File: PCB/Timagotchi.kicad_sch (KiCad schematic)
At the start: 11 parts, among them J1 Conn_01x13_Pin, J2 Conn_01x02_Pin, SW1 SW_Omron_B3FS, SW2 SW_Omron_B3FS, SW3 SW_Omron_B3FS, SW4 SW_Omron_B3FS, SW5 SW_Omron_B3FS, SW6 SW_Omron_B3FS, U1 XIAO-ESP32-S3-Plus-SMD, U2 MAX98357A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

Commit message: puhcuhbuh
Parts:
- removed J1: Conn_01x13_Pin, Connector_JST:JST_SH_SM13B-SRSS-TB_1x13-1MP_P1.00mm_Horizontal, symbol Connector:Conn_01x13_Pin
- added J3: 2005280180, CON_2005280180_MOL, symbol FFC:2005280180
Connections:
- net +3.3V: now also J3.1
- net GND: now also J3.3, J3.P1, J3.P2
- net LCD_BL: now also J3.2
- net LCD_CS: now also J3.9
- net LCD_DC: now also J3.7
- net LCD_RST: now also J3.8
- net MOSI: now also J3.5
- net SCLK: now also J3.4
- net TP_INT: now also J3.15
- net TP_SCL: now also J3.13
- net TP_SDA: now also J3.14
- net +5V: now reaches U1.14 (VBUS)
- new net MISO: J3.6
- no-connect marks 7 -> 14
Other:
- note added: "Screen FFC connector"
- note removed: "Screen Connector"

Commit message: optimizations and other stuff.
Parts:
- removed SW4, SW5, SW6: SW_Omron_B3FS, Button_Switch_SMD:SW_SPST_Omron_B3FS-100xP, symbol Switch:SW_Omron_B3FS
- J3: footprint CON_2005280180_MOL -> Connector_FFC-FPC:Molex_200528-0180_1x18-1MP_P1.00mm_Horizontal
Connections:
- net SD_CS is gone; now on net MOSI: U1.2 (GPIO2_A1_D1)
- net SW4 is gone; now on net LCD_CS: U1.18 (GPIO41_PDM_DATA_RX1)
- net SW5 is gone; now on net HPOS: U1.19 (GPIO42_PDM_CLK_TX1)
- net SW6 is gone; now on net VPOS: U1.20 (GPIO10_XMCLK_ADC_BAT)
- net TP_RST is gone; now on net I2S_SD: U1.10 (GPIO8_A9_D9_MISO)
- net HPOS: no longer U1.28 (GPIO42_MTMS_PDM_CLK_TX1)
- net I2S_SCK: now also U1.22 (GPIO12_DVP_Y7_SPI_MISO1); no longer U1.16 (GPIO39_CAM_SCL_I2S_SCK)
- net I2S_SD: no longer U1.15 (GPIO38_DVP_VSYNC_I2S_SD)
- net I2S_WS: now also U1.9 (GPIO7_A8_D8_SCK); no longer U1.17 (GPIO40_CAM_SDA_I2S_WS)
- net LCD_CS: no longer U1.8 (GPIO44_D7_RX)
- net MOSI: no longer U1.11 (GPIO9_A10_D10_MOSI)
- net SCLK: now also U1.17 (GPIO40_CAM_SDA_I2S_WS); no longer U1.9 (GPIO7_A8_D8_SCK)
- net SEL: now also U1.11 (GPIO9_A10_D10_MOSI); no longer U1.25 (GPIO40_MTDO_CAM_SDA_I2S_WS)
- net SW1: now also U1.8 (GPIO44_D7_RX); no longer U1.21 (GPIO11_DVP_Y8_SPI_MOSI1)
- net SW2: now also U1.21 (GPIO11_DVP_Y8_SPI_MOSI1); no longer U1.22 (GPIO12_DVP_Y7_SPI_MISO1)
- net VPOS: no longer U1.29 (GPIO39_MTCK_CAM_SCL_I2S_SCK)
- no-connect marks 14 -> 17

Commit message: Pcb changes, mostly files and 3d models.
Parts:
- removed U3: COM-09032, Joystick footprint:XDCR_COM-09032, symbol COM-09032:COM-09032
- added J1: Conn_01x04, Library:JOYSTICK-PSP1000, symbol Connector_Generic:Conn_01x04
- ScreenConnector: renamed from J3; footprint Connector_FFC-FPC:Molex_200528-0180_1x18-1MP_P1.00mm_Horizontal -> FFC:CON_2005280180_MOL
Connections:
- net +3.3V: now also J1.4 (Pin_4)
- net GND: now also J1.2 (Pin_2)
- net HPOS: now also U1.20 (GPIO10_XMCLK_ADC_BAT), J1.1 (Pin_1); no longer U1.19 (GPIO42_PDM_CLK_TX1)
- net VPOS: now also U1.19 (GPIO42_PDM_CLK_TX1), J1.3 (Pin_3); no longer U1.20 (GPIO10_XMCLK_ADC_BAT)
- net SEL: no longer names the net of U1.11 (GPIO9_A10_D10_MOSI)
- no-connect marks 17 -> 18

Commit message: puh cuh buh 2
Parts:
- renumbered ScreenConnector to ScreenConnector1
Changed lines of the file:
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@@
 		(dnp no)
 		(fields_autoplaced yes)
-		(property "Reference" "ScreenConnector"
+		(property "Reference" "ScreenConnector1"
 			(at 171.45 53.3399 0)
 			(show_name no)
@@
 			(project "Timagotchi"
 				(path "/fffb594e-bf77-45e9-a4da-34b8c4c79703"
-					(reference "ScreenConnector")
+					(reference "ScreenConnector1")
 					(unit 1)
 				)

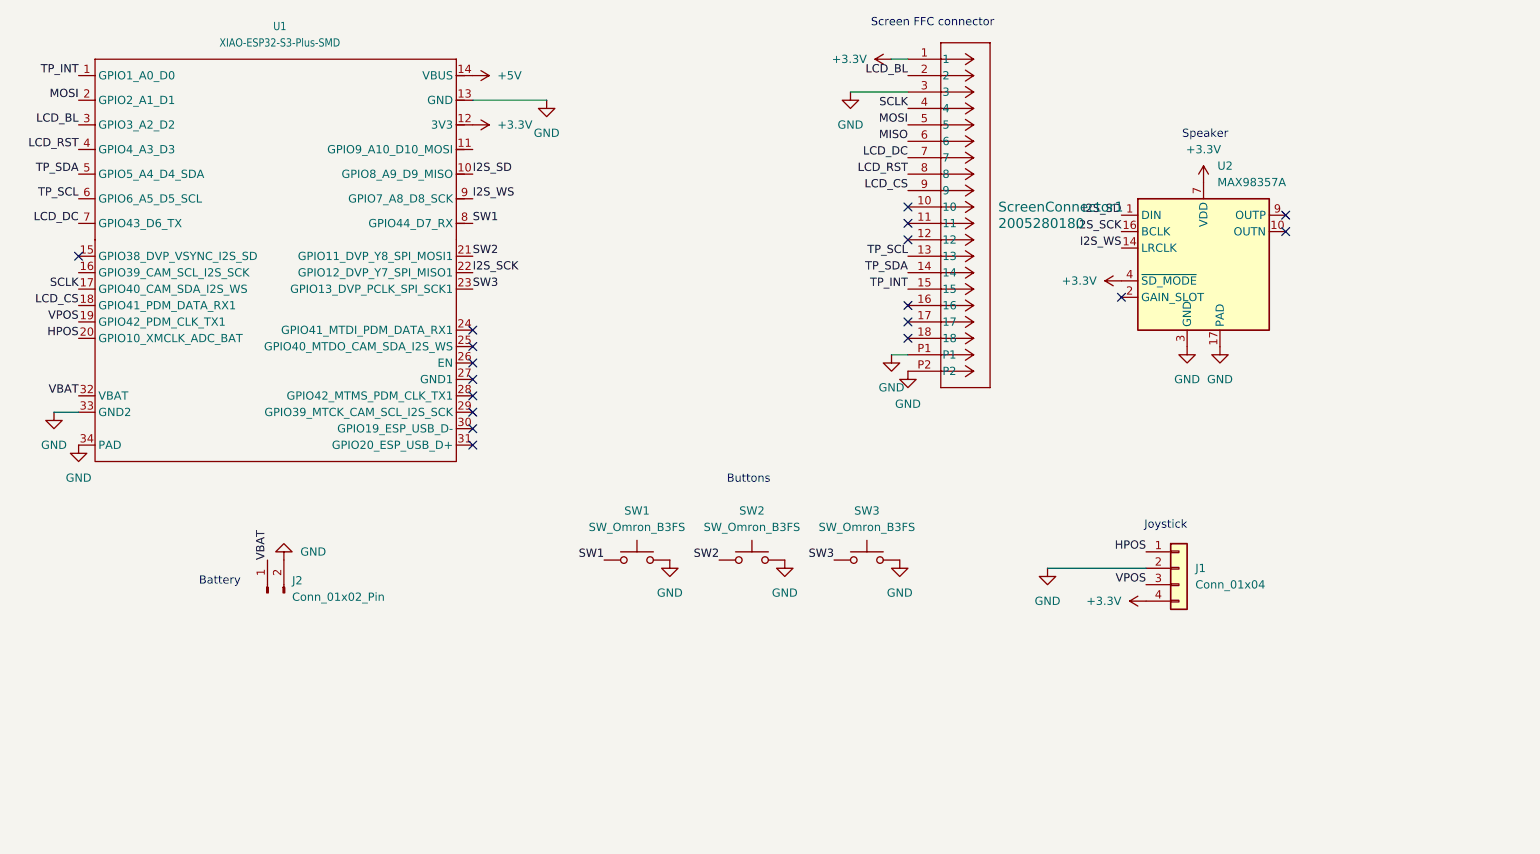
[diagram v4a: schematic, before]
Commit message: wiring and new speaker
added CMS-201438-058S
speaker and new gpio wiring
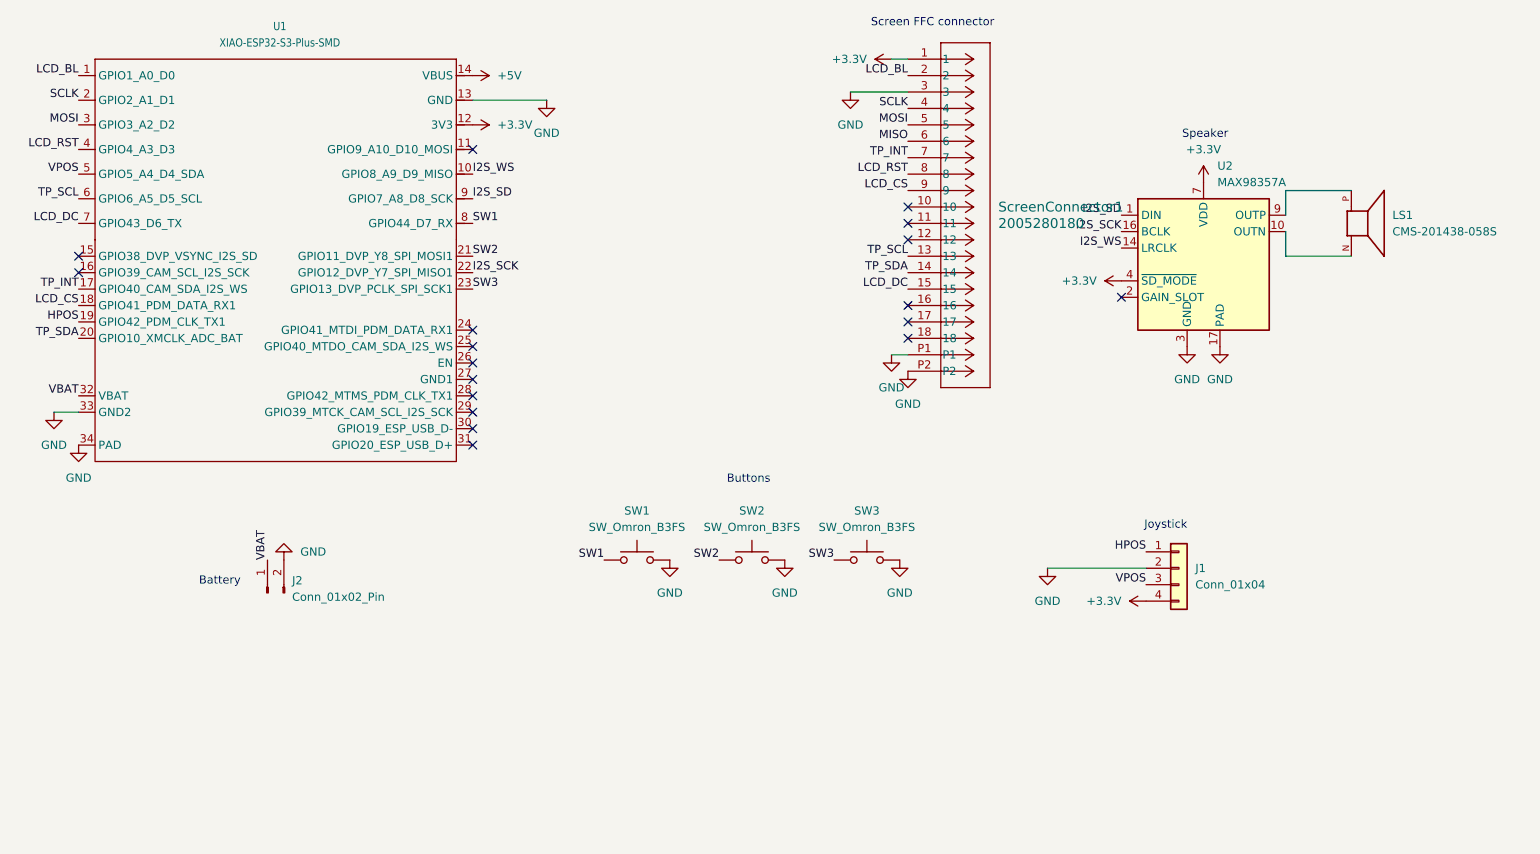
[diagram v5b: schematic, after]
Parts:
- added LS1: CMS-201438-058S, Speaker speaker:SPKR_CMS-201438-058S, symbol CMS-201438-058S:CMS-201438-058S
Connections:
- net HPOS: now also U1.19 (GPIO42_PDM_CLK_TX1); no longer U1.20 (GPIO10_XMCLK_ADC_BAT)
- net I2S_SD: now also U1.9 (GPIO7_A8_D8_SCK); no longer U1.10 (GPIO8_A9_D9_MISO)
- net I2S_WS: now also U1.10 (GPIO8_A9_D9_MISO); no longer U1.9 (GPIO7_A8_D8_SCK)
- net LCD_BL: now also U1.1 (GPIO1_A0_D0); no longer U1.3 (GPIO3_A2_D2)
- net LCD_DC: now also ScreenConnector1.15; no longer ScreenConnector1.7
- net MOSI: now also U1.3 (GPIO3_A2_D2); no longer U1.2 (GPIO2_A1_D1)
- net SCLK: now also U1.2 (GPIO2_A1_D1); no longer U1.17 (GPIO40_CAM_SDA_I2S_WS)
- net TP_INT: now also ScreenConnector1.7, U1.17 (GPIO40_CAM_SDA_I2S_WS); no longer ScreenConnector1.15, U1.1 (GPIO1_A0_D0)
- net TP_SDA: now also U1.20 (GPIO10_XMCLK_ADC_BAT); no longer U1.5 (GPIO5_A4_D4_SDA)
- net VPOS: now also U1.5 (GPIO5_A4_D4_SDA); no longer U1.19 (GPIO42_PDM_CLK_TX1)
- net at U2.10 (OUTN): now also LS1.N
- net at U2.9 (OUTP): now also LS1.P
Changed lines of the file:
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@@
-	)
-	(no_connect
-		(at 215.9 54.61)
 	)
 	(no_connect
@@
 	)
 	(no_connect
-		(at 215.9 57.15)
-	)
-	(no_connect
 		(at 157.48 53.34)
 	)
@@
 	(no_connect
 		(at 90.17 87.63)
+	)
+	(no_connect
+		(at 90.17 44.45)
+	)
+	(no_connect
+		(at 29.21 63.5)
 	)
 	(no_connect
@@
 	(wire
 		(pts
-			(xy 154.94 76.2) (xy 157.48 76.2)
+			(xy 215.9 54.61) (xy 215.9 50.8)
 		)
 		(stroke
@@
 	(wire
 		(pts
-			(xy 25.4 85.09) (xy 29.21 85.09)
+			(xy 215.9 60.96) (xy 215.9 57.15)
 		)
 		(stroke
@@
 	(wire
 		(pts
-			(xy 148.59 35.56) (xy 157.48 35.56)
+			(xy 154.94 76.2) (xy 157.48 76.2)
 		)
 		(stroke
@@
 		)
 	)
+	(wire
+		(pts
+			(xy 215.9 50.8) (xy 226.06 50.8)
+		)
+		(stroke
+			(width 0)
+			(type default)
+		)
+	)
+	(wire
+		(pts
+			(xy 25.4 85.09) (xy 29.21 85.09)
+		)
+		(stroke
+			(width 0)
+			(type default)
+		)
+	)
+	(wire
+		(pts
+			(xy 148.59 35.56) (xy 157.48 35.56)
+		)
+		(stroke
+			(width 0)
+			(type default)
+		)
+	)
+	(wire
+		(pts
+			(xy 226.06 60.96) (xy 215.9 60.96)
+		)
+		(stroke
+			(width 0)
+			(type default)
+		)
+	)
 	(label "VBAT"
 		(at 29.21 82.55 180)
@@
 		)
 	)
-	(label "SCLK"
+	(label "TP_INT"
 		(at 29.21 66.04 180)
 		(effects
@@
 		)
 	)
-	(label "HPOS"
+	(label "TP_SDA"
 		(at 29.21 73.66 180)
 		(effects
@@
 		)
 	)
+	(label "MOSI"
+		(at 29.21 40.64 180)
+		(effects
+			(font
+				(size 1.27 1.27)
+			)
+			(justify right bottom)
+		)
+	)
 	(label "LCD_BL"
-		(at 29.21 40.64 180)
+		(at 29.21 33.02 180)
 		(effects
 			(font
@@
 		)
 	)
-	(label "TP_INT"
-		(at 29.21 33.02 180)
-		(effects
-			(font
-				(size 1.27 1.27)
-			)
-			(justify right bottom)
-		)
-	)
-	(label "I2S_WS"
+	(label "I2S_SD"
 		(at 90.17 52.07 0)
 		(effects
@@
 		)
 	)
-	(label "LCD_DC"
+	(label "TP_INT"
 		(at 157.48 45.72 180)
 		(effects
@@
 		)
 	)
-	(label "TP_INT"
+	(label "LCD_DC"
 		(at 157.48 66.04 180)
 		(effects
@@
 		)
 	)
-	(label "TP_SDA"
+	(label "VPOS"
 		(at 29.21 48.26 180)
 		(effects
@@
 		)
 	)
-	(label "MOSI"
+	(label "SCLK"
 		(at 29.21 36.83 180)
 		(effects
@@
 		)
 	)
-	(label "VPOS"
+	(label "HPOS"
 		(at 29.21 71.12 180)
 		(effects
@@
 		)
 	)
-	(label "I2S_SD"
+	(label "I2S_WS"
 		(at 90.17 48.26 0)
 		(effects
@@
 					(unit 1)
 				)
+			)
+		)
+	)
+	(symbol
+		(lib_id "CMS-201438-058S:CMS-201438-058S")
+		(at 228.6 55.88 0)
+		(unit 1)
+		(body_style 1)
+		(exclude_from_sim no)
+		(in_bom yes)
+		(on_board yes)
+		(in_pos_files yes)
+		(dnp no)
+		(fields_autoplaced yes)
+		(property "Reference" "LS1"
+			(at 232.41 54.6099 0)
+			(show_name no)
+			(do_not_autoplace no)
+			(effects
+				(font
+					(size 1.27 1.27)
+				)
+				(justify left)
+			)
+		)
+		(property "Value" "CMS-201438-058S"
+			(at 232.41 57.1499 0)
+			(show_name no)
+			(do_not_autoplace no)
+			(effects
+				(font
+					(size 1.27 1.27)
+				)
+				(justify left)
+			)
+		)
+		(property "Footprint" "Speaker speaker:SPKR_CMS-201438-058S"
+			(at 228.6 55.88 0)
+			(hide yes)
+			(show_name no)
+			(do_not_autoplace no)
+			(effects
+				(font
+					(size 1.27 1.27)
+				)
+				(justify bottom)
+			)
+		)
+		(property "Datasheet" ""
+			(at 228.6 55.88 0)
+			(hide yes)
+			(show_name no)
+			(do_not_autoplace no)
+			(effects
+				(font
+					(size 1.27 1.27)
+				)
+			)
+		)
+		(property "Description" ""
+			(at 228.6 55.88 0)
+			(hide yes)
+			(show_name no)
+			(do_not_autoplace no)
+			(effects
+				(font
+					(size 1.27 1.27)
+				)
+			)
+		)
+		(property "MAXIMUM_PACKAGE_HEIGHT" "4.1mm"
+			(at 228.6 55.88 0)
+			(hide yes)
+			(show_name no)
+			(do_not_autoplace no)
+			(effects
+				(font
+					(size 1.27 1.27)
+				)
+				(justify bottom)
+			)
+		)
+		(property "CREATOR" "DIZAR"
+			(at 228.6 55.88 0)
+			(hide yes)
+			(show_name no)
+			(do_not_autoplace no)
+			(effects
+				(font
+					(size 1.27 1.27)
+				)
+				(justify bottom)
+			)
+		)
+		(property "STANDARD" "Manufacturer Recommendations"
+			(at 228.6 55.88 0)
+			(hide yes)
+			(show_name no)
+			(do_not_autoplace no)
+			(effects
+				(font
+					(size 1.27 1.27)
+				)
+				(justify bottom)
+			)
+		)
+		(property "PARTREV" "1.03"
+			(at 228.6 55.88 0)
+			(hide yes)
+			(show_name no)
+			(do_not_autoplace no)
+			(effects
+				(font
+					(size 1.27 1.27)
+				)
+				(justify bottom)
+			)
+		)
+		(property "VERIFIER" ""
+			(at 228.6 55.88 0)
+			(hide yes)
+			(show_name no)
+			(do_not_autoplace no)
+			(effects
+				(font
+					(size 1.27 1.27)
+				)
+				(justify bottom)
+			)
+		)
+		(property "MANUFACTURER" "Same Sky"
+			(at 228.6 55.88 0)
+			(hide yes)
+			(show_name no)
+			(do_not_autoplace no)
+			(effects
+				(font
+					(size 1.27 1.27)
+				)
+				(justify bottom)
+			)
+		)
+		(pin "N"
+		)
+		(pin "P"
+		)
+		(instances
+			(project "Timagotchi"
+				(path "/fffb594e-bf77-45e9-a4da-34b8c4c79703"
+					(reference "LS1")
+					(unit 1)
+				)

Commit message: PCB UHH delete later maybe
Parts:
- removed J1: Conn_01x04, Library:JOYSTICK-PSP1000, symbol Connector_Generic:Conn_01x04
- removed SW1, SW2, SW3: SW_Omron_B3FS, Button_Switch_SMD:SW_SPST_Omron_B3FS-100xP, symbol Switch:SW_Omron_B3FS
- added S1, S2, S3, S4, S5: TL3342F160QG, Switch Footprints:SW_TL3342F160QG, symbol TL3342F160QG:TL3342F160QG
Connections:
- net GND: now also S1.3, S1.4, S2.3, S2.4, S3.3, S3.4, S4.3, S4.4, S5.3, S5.4
- net SW1: now also U1.11 (GPIO9_A10_D10_MOSI), S1.1, S1.2; no longer U1.8 (GPIO44_D7_RX)
- net SW2: now also U1.8 (GPIO44_D7_RX), S2.1, S2.2; no longer U1.21 (GPIO11_DVP_Y8_SPI_MOSI1)
- net SW3: now also U1.21 (GPIO11_DVP_Y8_SPI_MOSI1), S3.1, S3.2; no longer U1.23 (GPIO13_DVP_PCLK_SPI_SCK1)
- net HPOS: no longer names the net of U1.19 (GPIO42_PDM_CLK_TX1)
- net VPOS renamed SW5
- net SW5: now also S5.1, S5.2
- new net SW4: S4.1, S4.2, U1.23 (GPIO13_DVP_PCLK_SPI_SCK1)
- no-connect marks 18 -> 17
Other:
- note added: "Directional Pad"
- note removed: "Buttons"
- note removed: "Joystick"

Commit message: lots of stuff
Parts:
- added C1: 100nF, Capacitor_SMD:C_0805_2012Metric_Pad1.18x1.45mm_HandSolder, symbol Device:C
- added C2: 10µF, Capacitor_SMD:C_0805_2012Metric_Pad1.18x1.45mm_HandSolder, symbol Device:C
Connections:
- net +3.3V: now also C1.1, C2.1; no longer U2.4 (~{SD_MODE}), U2.7 (VDD), U2.8 (VDD)
- net GND: now also C2.2
- net SD_MODE: now reaches U1.15 (GPIO38_DVP_VSYNC_I2S_SD)
- net SD_MODE: now also U2.4 (~{SD_MODE})
- new net: C1.2, U2.7 (VDD), U2.8 (VDD)
- no-connect marks 17 -> 16

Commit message: Power flags and a nc symbol
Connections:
- no-connect marks 16 -> 17
